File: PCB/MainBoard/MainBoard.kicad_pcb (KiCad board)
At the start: 2 copper layers, 21 parts, among them Q1 PT334, Q2 BC327, SW2 SW_DIP_x05, U1 LM393N

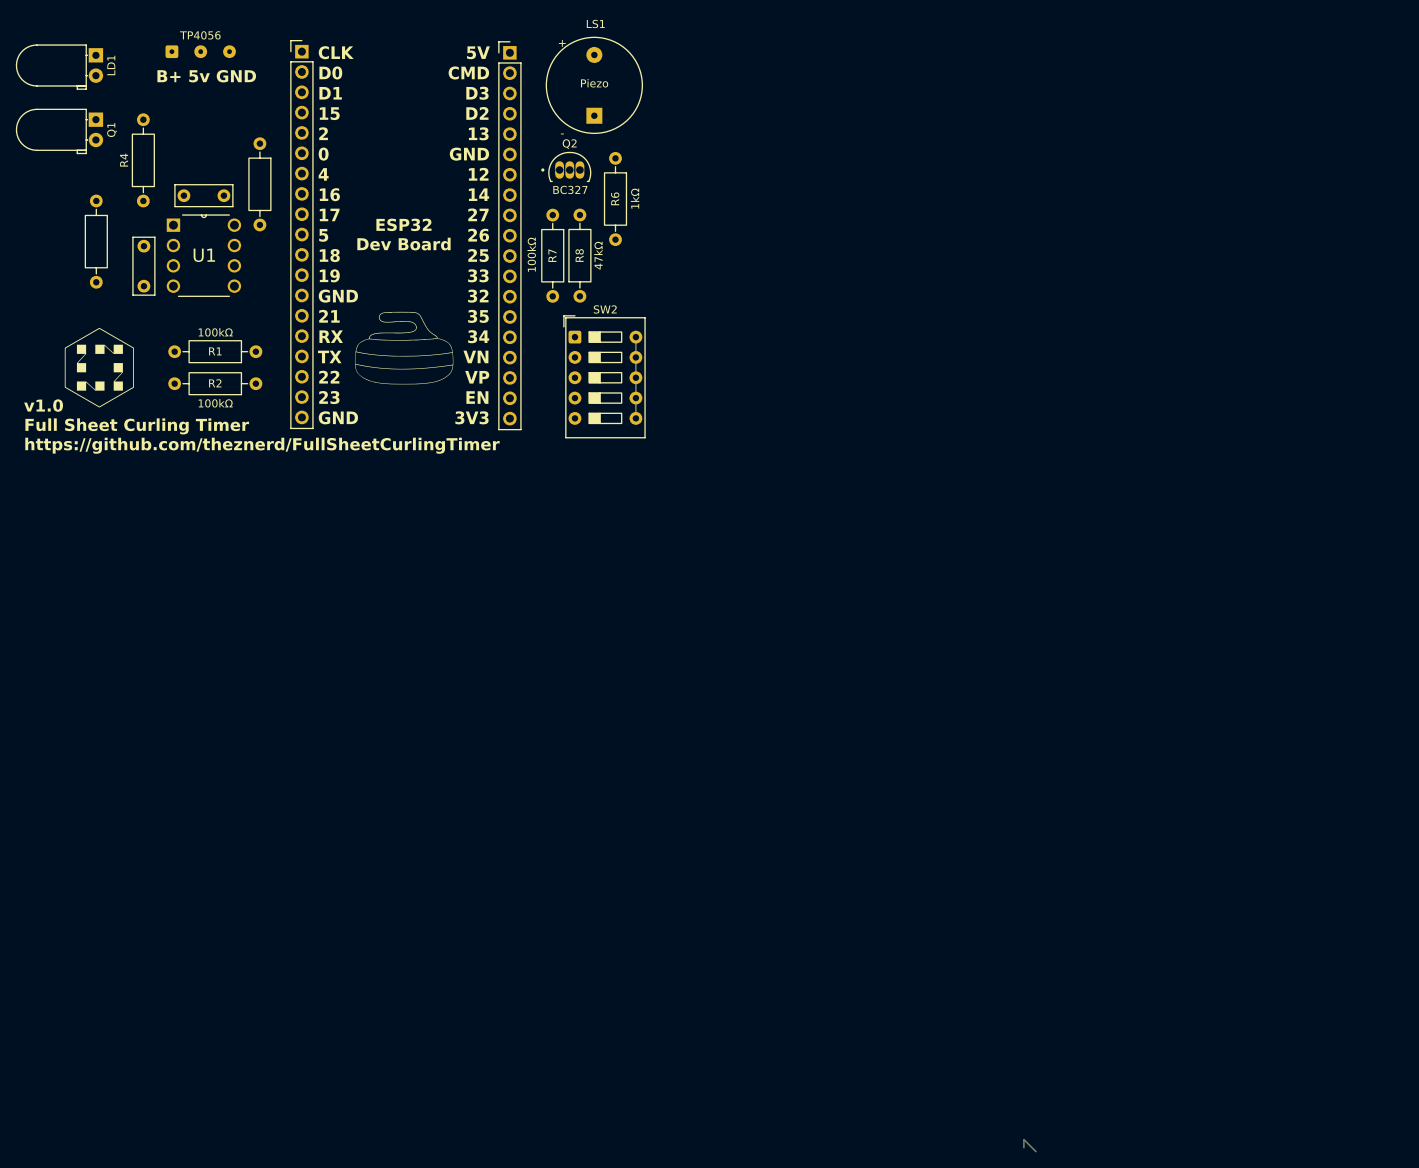
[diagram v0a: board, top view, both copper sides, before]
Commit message: PCB v1.0 - schematic needs review still in comparison to PCB - initial order of PCBs with JLCPCB. Updated BOM to reflect actual resistor/capacitor count.
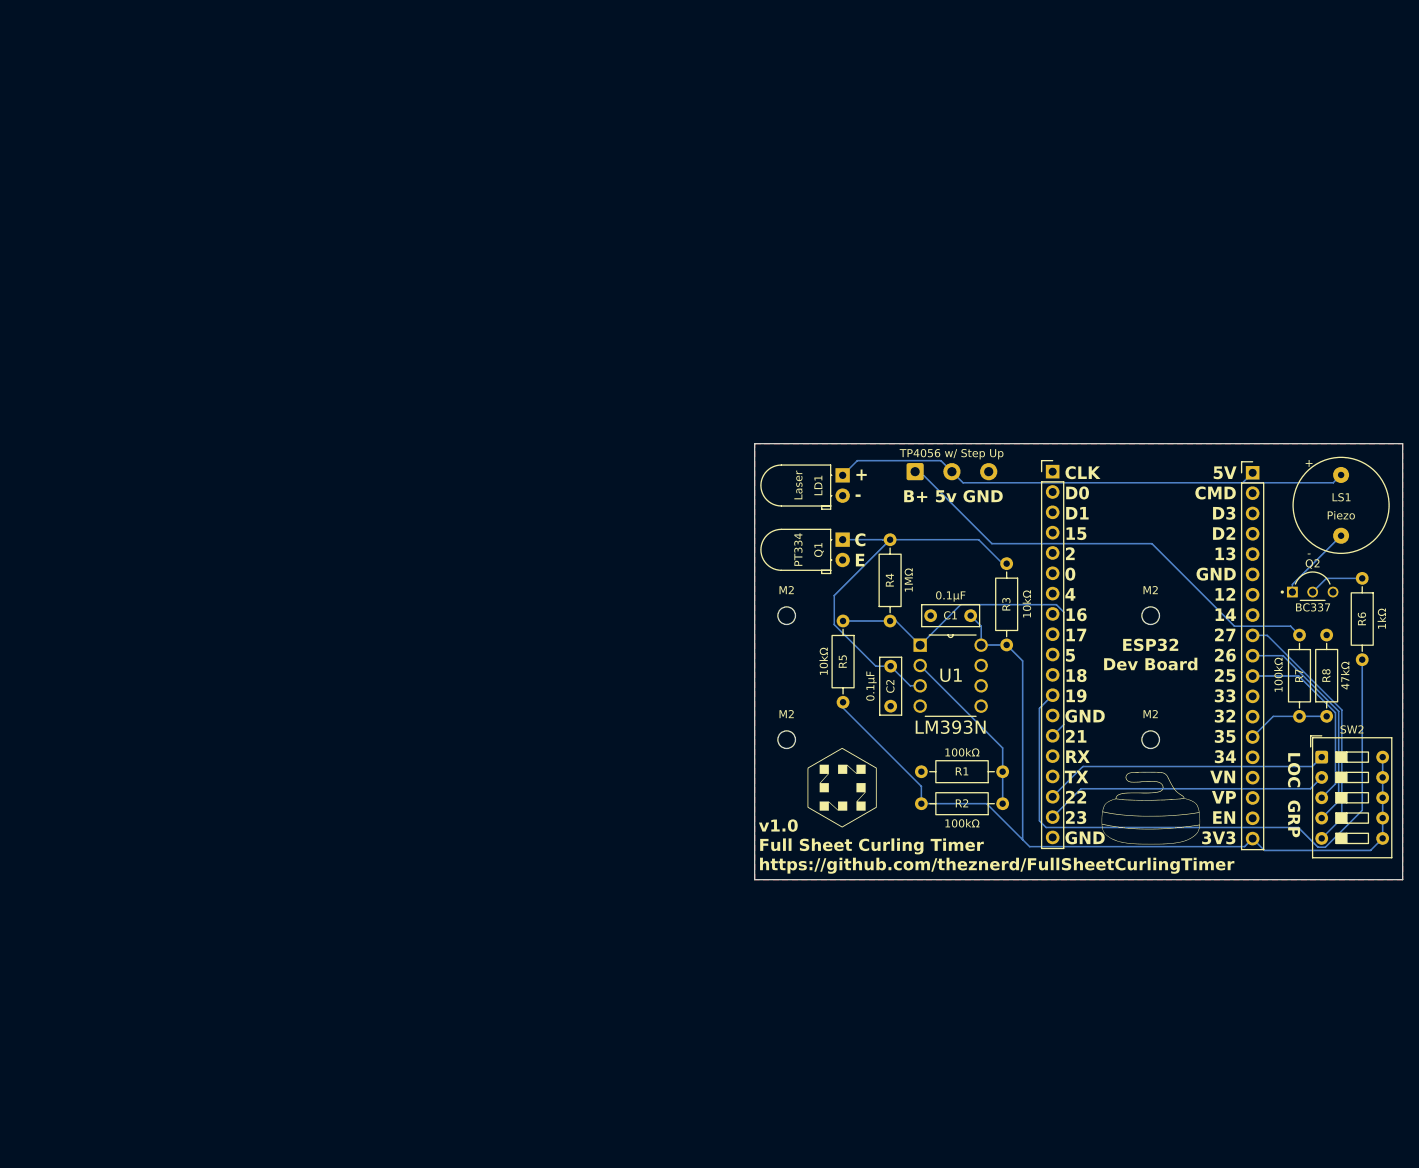
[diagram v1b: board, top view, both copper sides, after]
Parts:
- added M2: MountingHole_2.2mm_M2, MountingHole:MountingHole_2.2mm_M2, F.Cu at (158.8, 101.0)
- added M2: MountingHole_2.2mm_M2, MountingHole:MountingHole_2.2mm_M2, F.Cu at (113.3, 116.5)
- added M2: MountingHole_2.2mm_M2, MountingHole:MountingHole_2.2mm_M2, F.Cu at (158.8, 116.5)
- added M2: MountingHole_2.2mm_M2, MountingHole:MountingHole_2.2mm_M2, F.Cu at (113.3, 101.0)
- Q2: value BC327 -> BC337; footprint FSCT:TO92127P476H533-3 -> FSCT:TO92254P480H870-3
- TP4056 w/ Step Up: renamed from TP4056; value SolderWire-0.1sqmm_1x03_P3.6mm_D0.4mm_OD1mm -> SolderWire-0.5sqmm_1x03_P4.6mm_D0.9mm_OD2.1mm; footprint Connector_Wire:SolderWire-0.1sqmm_1x03_P3.6mm_D0.4mm_OD1mm -> Connector_Wire:SolderWire-0.5sqmm_1x03_P4.6mm_D0.9mm_OD2.1mm
- moved G*** 109.6 mm to (158.8, 125.0)
- moved   107.5 mm to (146.6, 83.0)
- moved R6 107.1 mm to (185.3, 96.3)
- moved C1 107.1 mm to (136.3, 101.0)
- moved C2 107.1 mm to (126.3, 107.3)
- moved LD1 107.1 mm to (120.3, 83.5)
- moved LS1 107.1 mm to (182.6, 87.2)
- moved Q1 107.1 mm to (120.3, 91.5)
- moved R1 107.1 mm to (140.3, 120.5)
- moved R2 107.1 mm to (140.3, 124.5)
- moved R3 107.1 mm to (140.8, 94.5)
- moved R4 107.1 mm to (126.3, 101.7)
- moved R5 107.1 mm to (120.4, 101.7)
- moved R7 107.1 mm to (177.4, 103.4)
- moved R8 107.1 mm to (180.8, 113.6)
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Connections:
-   pad 12: (no net) -> Net-(R6-Pad2)
-   pad 14: (no net) -> Net-(R4-Pad1)
- LD1 pad 1: GND -> +5V In PCB
- LD1 pad 2: +5V In PCB -> GND
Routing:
- net +3V3: track 10.2 -> 121.0 mm
- net Net-(R6-Pad2): track 0.00 -> 78.9 mm
- net +5V In PCB: track 0.00 -> 66.4 mm
- net Net-(R7-Pad1): track 0.00 -> 56.5 mm
- net Net-(Q1-C): track 0.00 -> 49.2 mm
- net Net-(R4-Pad1): track 0.00 -> 47.4 mm
- net Net-(SW2-Pad2): track 0.00 -> 35.7 mm
- net Net-(SW2-Pad1): track 0.00 -> 35.7 mm
- net Net-(SW2-Pad5): track 0.00 -> 32.1 mm
- net Net-(SW2-Pad4): track 0.00 -> 27.9 mm
- net Net-(SW2-Pad3): track 0.00 -> 23.6 mm
- net Net-(U1A--): track 0.00 -> 21.5 mm
- net Net-(R7-Pad2): track 0.00 -> 10.3 mm
- net Net-(Q2-C): track 0.00 -> 9.56 mm
- net Net-(Q2-B): track 0.00 -> 6.90 mm
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- added copper zone on F.Cu, net GND
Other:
- board outline added: 81 x 54.5 mm
- board text added: "+ -"
- board text added: "C E"
- board text added: "GRP"
- board text added: "LOC"

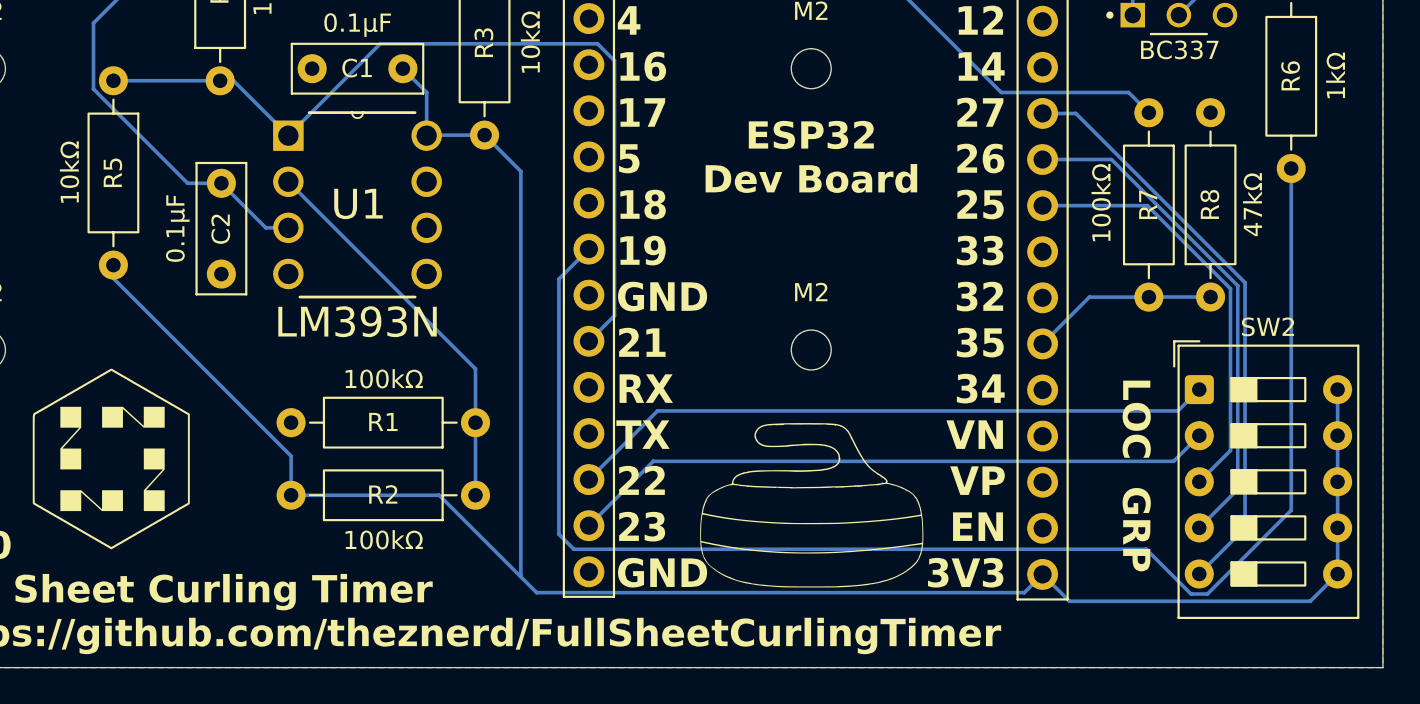
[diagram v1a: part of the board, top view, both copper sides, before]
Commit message: Ran into issues in breadboarding - hoping r2 of PCB fixes. Luckily caught the order in time to get new files uploaded so order was not wasted.
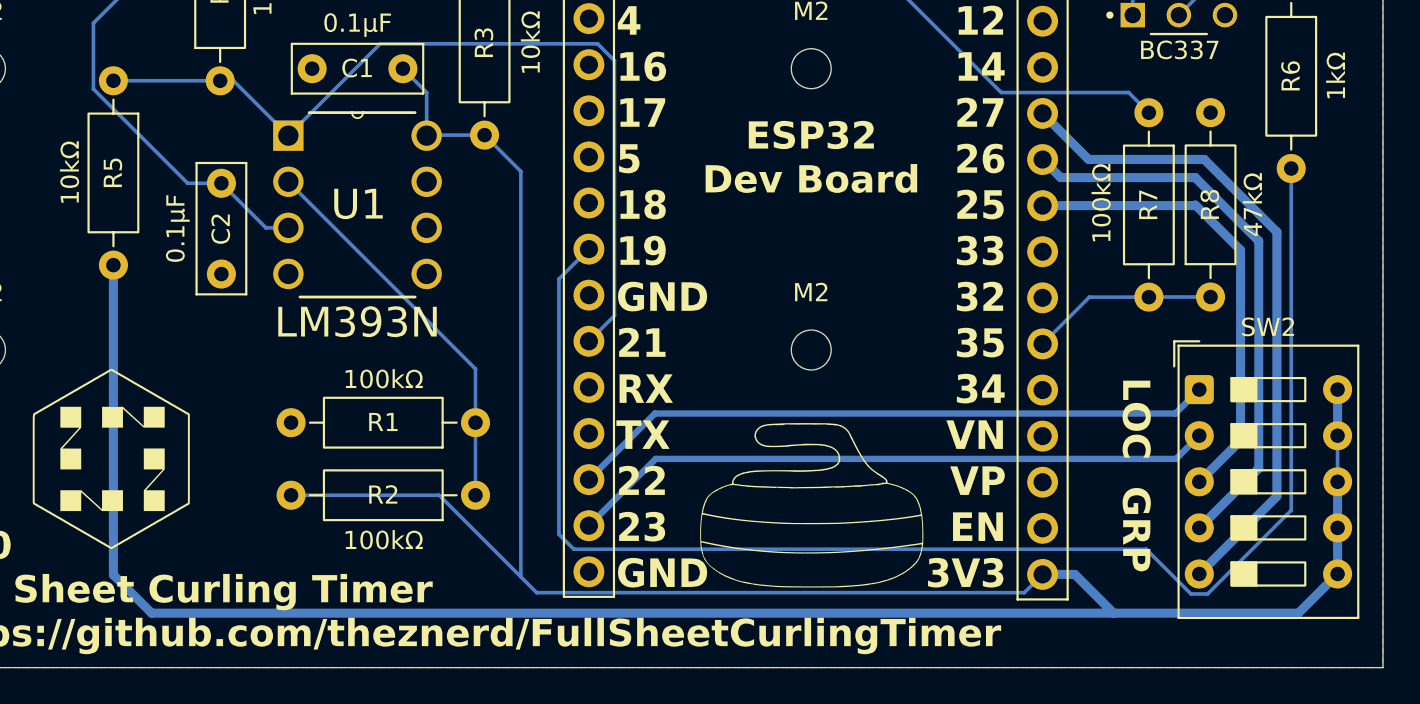
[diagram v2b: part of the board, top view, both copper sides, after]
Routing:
- net +3V3: track 121.0 -> 177.9 mm
- net Net-(SW2-Pad5): track 32.1 -> 36.2 mm
- net Net-(SW2-Pad4): track 27.9 -> 30.9 mm
- net Net-(SW2-Pad3): track 23.6 -> 25.7 mm
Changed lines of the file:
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@@
 	)
 	(segment
-		(start 130.18276 122.34)
-		(end 130.18276 124.503094)
-		(width 0.2)
-		(layer "B.Cu")
-		(net 2)
-	)
-	(segment
-		(start 187.84276 128.841305)
-		(end 186.34076 130.343305)
-		(width 0.2)
+		(start 120.393437 111.823827)
+		(end 120.393437 128.893437)
+		(width 0.5)
+		(layer "B.Cu")
+		(net 2)
+	)
+	(segment
+		(start 122.5 131)
+		(end 175.5 131)
+		(width 0.5)
+		(layer "B.Cu")
+		(net 2)
+	)
+	(segment
+		(start 175.5 131)
+		(end 185.684065 131)
+		(width 0.5)
 		(layer "B.Cu")
 		(net 2)
@@
 		(start 187.84276 126.301305)
 		(end 187.84276 123.761305)
-		(width 0.2)
-		(layer "B.Cu")
-		(net 2)
-	)
-	(segment
-		(start 186.34076 130.343305)
-		(end 173.068305 130.343305)
-		(width 0.2)
+		(width 0.5)
+		(layer "B.Cu")
+		(net 2)
+	)
+	(segment
+		(start 120.393437 128.893437)
+		(end 122.5 131)
+		(width 0.5)
 		(layer "B.Cu")
 		(net 2)
@@
 	)
 	(segment
-		(start 173.068305 130.343305)
-		(end 171.59 128.865)
-		(width 0.2)
-		(layer "B.Cu")
-		(net 2)
-	)
-	(segment
 		(start 140.84276 104.66)
 		(end 137.68276 104.66)
@@
 	)
 	(segment
-		(start 120.393437 111.823827)
-		(end 120.393437 112.550677)
-		(width 0.2)
+		(start 185.684065 131)
+		(end 187.84276 128.841305)
+		(width 0.5)
 		(layer "B.Cu")
 		(net 2)
@@
 		(start 187.84276 128.841305)
 		(end 187.84276 126.301305)
-		(width 0.2)
+		(width 0.5)
 		(layer "B.Cu")
 		(net 2)
@@
 	)
 	(segment
-		(start 120.393437 112.550677)
-		(end 130.18276 122.34)
-		(width 0.2)
+		(start 171.59 128.865)
+		(end 173.365 128.865)
+		(width 0.5)
 		(layer "B.Cu")
 		(net 2)
@@
 	)
 	(segment
+		(start 173.365 128.865)
+		(end 175.5 131)
+		(width 0.5)
+		(layer "B.Cu")
+		(net 2)
+	)
+	(segment
 		(start 187.84276 121.221305)
 		(end 187.84276 118.681305)
-		(width 0.2)
+		(width 0.5)
 		(layer "B.Cu")
 		(net 2)
@@
 	)
 	(segment
-		(start 180.22276 123.761305)
-		(end 181.94376 122.040305)
-		(width 0.2)
+		(start 182.5 121.484065)
+		(end 180.22276 123.761305)
+		(width 0.5)
 		(layer "B.Cu")
 		(net 11)
 	)
 	(segment
+		(start 179.955 108.545)
+		(end 180 108.5)
+		(width 0.2)
+		(layer "B.Cu")
+		(net 11)
+	)
+	(segment
 		(start 171.59 108.545)
-		(end 177.36481 108.545)
-		(width 0.2)
+		(end 179.955 108.545)
+		(width 0.5)
 		(layer "B.Cu")
 		(net 11)
 	)
 	(segment
-		(start 181.94376 122.040305)
-		(end 181.94376 113.12395)
-		(width 0.2)
+		(start 180 108.5)
+		(end 182.5 111)
+		(width 0.5)
 		(layer "B.Cu")
 		(net 11)
 	)
 	(segment
-		(start 181.94376 113.12395)
-		(end 177.36481 108.545)
-		(width 0.2)
+		(start 182.5 111)
+		(end 182.5 121.484065)
+		(width 0.5)
 		(layer "B.Cu")
 		(net 11)
 	)
 	(segment
-		(start 150.37676 119.856)
-		(end 179.048065 119.856)
-		(width 0.2)
+		(start 150.23276 120)
+		(end 146.59276 123.64)
+		(width 0.35)
 		(layer "B.Cu")
 		(net 12)
 	)
 	(segment
-		(start 179.048065 119.856)
-		(end 180.22276 118.681305)
-		(width 0.2)
+		(start 180.22276 118.681305)
+		(end 178.904065 120)
+		(width 0.35)
 		(layer "B.Cu")
 		(net 12)
 	)
 	(segment
-		(start 146.59276 123.64)
-		(end 150.37676 119.856)
-		(width 0.2)
+		(start 178.904065 120)
+		(end 150.23276 120)
+		(width 0.35)
 		(layer "B.Cu")
 		(net 12)
 	)
 	(segment
-		(start 146.59276 126.18)
-		(end 150.13876 122.634)
-		(width 0.2)
+		(start 150.27276 122.5)
+		(end 146.59276 126.18)
+		(width 0.35)
 		(layer "B.Cu")
 		(net 13)
 	)
 	(segment
-		(start 178.810065 122.634)
-		(end 180.22276 121.221305)
-		(width 0.2)
+		(start 178.944065 122.5)
+		(end 150.27276 122.5)
+		(width 0.35)
 		(layer "B.Cu")
 		(net 13)
 	)
 	(segment
-		(start 150.13876 122.634)
-		(end 178.810065 122.634)
-		(width 0.2)
+		(start 180.22276 121.221305)
+		(end 178.944065 122.5)
+		(width 0.35)
 		(layer "B.Cu")
 		(net 13)
 	)
 	(segment
+		(start 183.5 110.5)
+		(end 183.5 123.024065)
+		(width 0.5)
+		(layer "B.Cu")
+		(net 14)
+	)
+	(segment
 		(start 171.59 106.005)
-		(end 175.39191 106.005)
-		(width 0.2)
+		(end 172.585 107)
+		(width 0.5)
 		(layer "B.Cu")
 		(net 14)
 	)
 	(segment
-		(start 182.34476 112.95785)
-		(end 175.39191 106.005)
-		(width 0.2)
+		(start 172.585 107)
+		(end 180 107)
+		(width 0.5)
 		(layer "B.Cu")
 		(net 14)
 	)
 	(segment
-		(start 180.22276 126.301305)
-		(end 182.34476 124.179305)
-		(width 0.2)
+		(start 180 107)
+		(end 183.5 110.5)
+		(width 0.5)
 		(layer "B.Cu")
 		(net 14)
 	)
 	(segment
-		(start 182.34476 124.179305)
-		(end 182.34476 112.95785)
-		(width 0.2)
+		(start 183.5 123.024065)
+		(end 180.22276 126.301305)
+		(width 0.5)
 		(layer "B.Cu")
 		(net 14)
 	)
 	(segment
+		(start 174.125 106)
+		(end 180.5 106)
+		(width 0.5)
+		(layer "B.Cu")
+		(net 15)
+	)
+	(segment
+		(start 184.5 110)
+		(end 184.5 124.564065)
+		(width 0.5)
+		(layer "B.Cu")
+		(net 15)
+	)
+	(segment
+		(start 180.5 106)
+		(end 184.5 110)
+		(width 0.5)
+		(layer "B.Cu")
+		(net 15)
+	)
+	(segment
 		(start 171.59 103.465)
-		(end 173.41901 103.465)
-		(width 0.2)
+		(end 174.125 106)
+		(width 0.5)
 		(layer "B.Cu")
 		(net 15)
 	)
 	(segment
-		(start 182.74576 126.318305)
+		(start 184.5 124.564065)
 		(end 180.22276 128.841305)
-		(width 0.2)
-		(layer "B.Cu")
-		(net 15)
-	)
-	(segment
-		(start 173.41901 103.465)
-		(end 182.74576 112.79175)
-		(width 0.2)
-		(layer "B.Cu")
-		(net 15)
-	)
-	(segment
-		(start 182.74576 112.79175)
-		(end 182.74576 126.318305)
-		(width 0.2)
+		(width 0.5)
 		(layer "B.Cu")
 		(net 15)
@@
 	)
 	(group ""
-		(members "065837ff-808d-4769-a222-3fa3dd4ed5d3" "0d9e8b25-23ec-4308-9117-eb1b87236902"
-			"106b5d3f-85bb-4db2-b020-27fd9d0702f7" "11d32808-9791-4147-9197-c40e630cf00e"
-			"1e53c75a-c400-4c70-afb8-79dcad06ab0b" "1f03db80-088d-47fb-997e-d0ea41886262"
-			"2201211f-2d85-4912-8850-66933c111e7c" "2d7c783d-3c27-46d9-94fb-51ed91fe8147"
+		(members "036c030a-104a-48e9-9ccc-71984e2faeae" "03a2a73d-10c4-40fc-ad21-b867e98f4821"
+			"065837ff-808d-4769-a222-3fa3dd4ed5d3" "106b5d3f-85bb-4db2-b020-27fd9d0702f7"
+			"11d32808-9791-4147-9197-c40e630cf00e" "14031820-b3a9-4c00-926b-9ff742a6e368"
+			"2b30c3bb-56e2-4df1-ab0b-fbca5a1da1e4" "2ef18e10-ab9c-4259-9140-622ea39c83b3"
 			"34b715ce-0581-4647-90f0-7f650661f19e" "400d3708-628a-4949-9212-72c7ab63d95b"
-			"50d2fee9-c65f-4ce8-b3c7-377433f4511f" "53f750a6-4e2b-4a7d-9710-b7a3d52da83b"
-			"552f3980-995f-44fe-b68b-7047c9190cc7" "573e2199-c05e-4cd3-811a-98c245c6ed63"
-			"5a79fcec-9a63-45e5-a101-524296644128" "69536c59-fff7-4e6b-a96a-d2e90b69dca2"
-			"6e6bef6c-e4f7-4da9-94ba-04563290ee98" "70fe938f-ae51-4f92-88c8-b4927a7e2549"
-			"7508f9c4-4f1b-4b3e-b2df-e6e23dc1d785" "7d2f4c7c-ec44-4ede-a1f1-26ce29945458"
-			"82ecf8ae-e87c-46de-8bfc-55f22019af6d" "8d086b9a-4fd8-41f2-8d3b-0619f062ab3a"
-			"95e8481d-76c6-4a67-bec3-ff43f6df77ce" "987540a4-9f79-4d11-866f-ce69cd87beca"
-			"9b5b4e9f-54a2-4c92-ab0e-c5b674d68659" "adea65d3-93c9-498e-91b8-a2070095deae"
-			"e384ecae-c1c1-4140-8f0e-89ae3f805ba3" "e9af4e38-ea17-4d91-97e9-386148d629ff"
-			"eaa86b0b-c892-4907-8a1b-1101dbefb537" "eb32fc49-4c55-41aa-b7f5-095a370cc291"
+			"41fdbaa8-07b7-4d05-a4ca-1f7e46c6bcf9" "43ed4bf7-efae-4596-9db1-31a113a5209d"
+			"4eb751a9-3366-4a01-b53f-386c3dadc9d2" "50d2fee9-c65f-4ce8-b3c7-377433f4511f"
+			"53cfe692-d203-4155-9c7e-1f1224e526f9" "6e6bef6c-e4f7-4da9-94ba-04563290ee98"
+			"70fe938f-ae51-4f92-88c8-b4927a7e2549" "7963d77c-36a3-4bba-ac4a-d77489a137f1"
+			"8d086b9a-4fd8-41f2-8d3b-0619f062ab3a" "95d24ec2-5295-4d44-be75-ada78334d88a"
+			"987540a4-9f79-4d11-866f-ce69cd87beca" "9b5b4e9f-54a2-4c92-ab0e-c5b674d68659"
+			"a01d0954-3d04-430e-bf3c-ea020ed0f2d6" "a8825382-07d9-4734-8ef5-615eaab89acb"
+			"b5d7da21-f8c1-4d64-833b-cf1a2b5f33b6" "c8abbfb5-41f1-4679-9696-4538afad587c"
+			"cdb7b929-4abc-4a92-8753-b82199a66b5b" "ce4d9001-b22b-4055-9859-13f6a6c46d95"
+			"e21c318f-47e3-4728-9c22-ebdd74b17491" "e384ecae-c1c1-4140-8f0e-89ae3f805ba3"
 			"eca16d80-8543-41d8-8388-3e93bb0092b7" "f01984ea-928b-49eb-8a6f-04ad3cccbb8c"
-			"f73c78e2-e177-4239-90af-a71558a118ee" "ff6bb1e2-481e-48e5-9ceb-aa6be5ca6468"
+			"f5954bb2-2576-4ea3-b59f-2848ab1f73e3" "f73c78e2-e177-4239-90af-a71558a118ee"
+			"f8814bc6-49b9-44a4-aa6f-daffbc239715" "fd988479-fed4-4749-becd-e9ad53effdf4"
+			"ff6bb1e2-481e-48e5-9ceb-aa6be5ca6468"
 		)
 	)
